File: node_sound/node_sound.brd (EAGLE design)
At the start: 74 x 74 mm, 8 parts, among them U1 TINY85-20-DIP

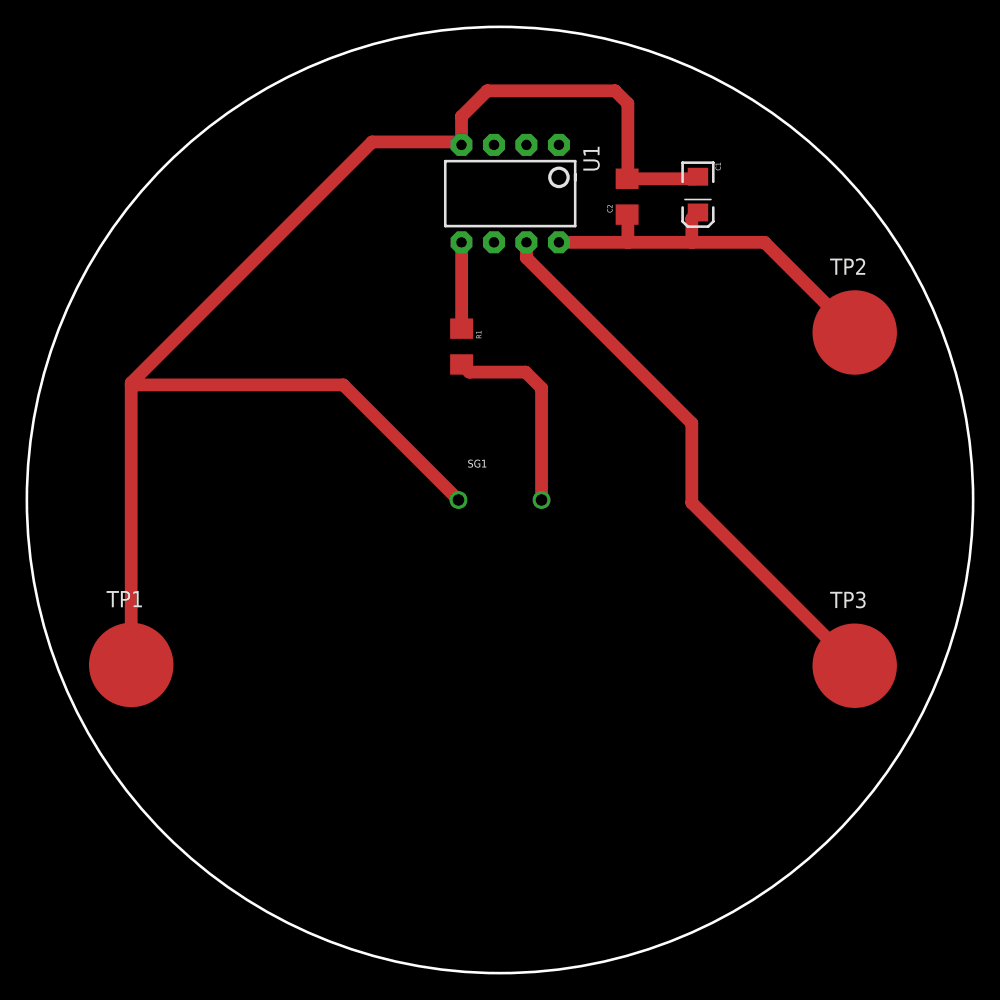
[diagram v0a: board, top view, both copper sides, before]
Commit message: Box dimension added
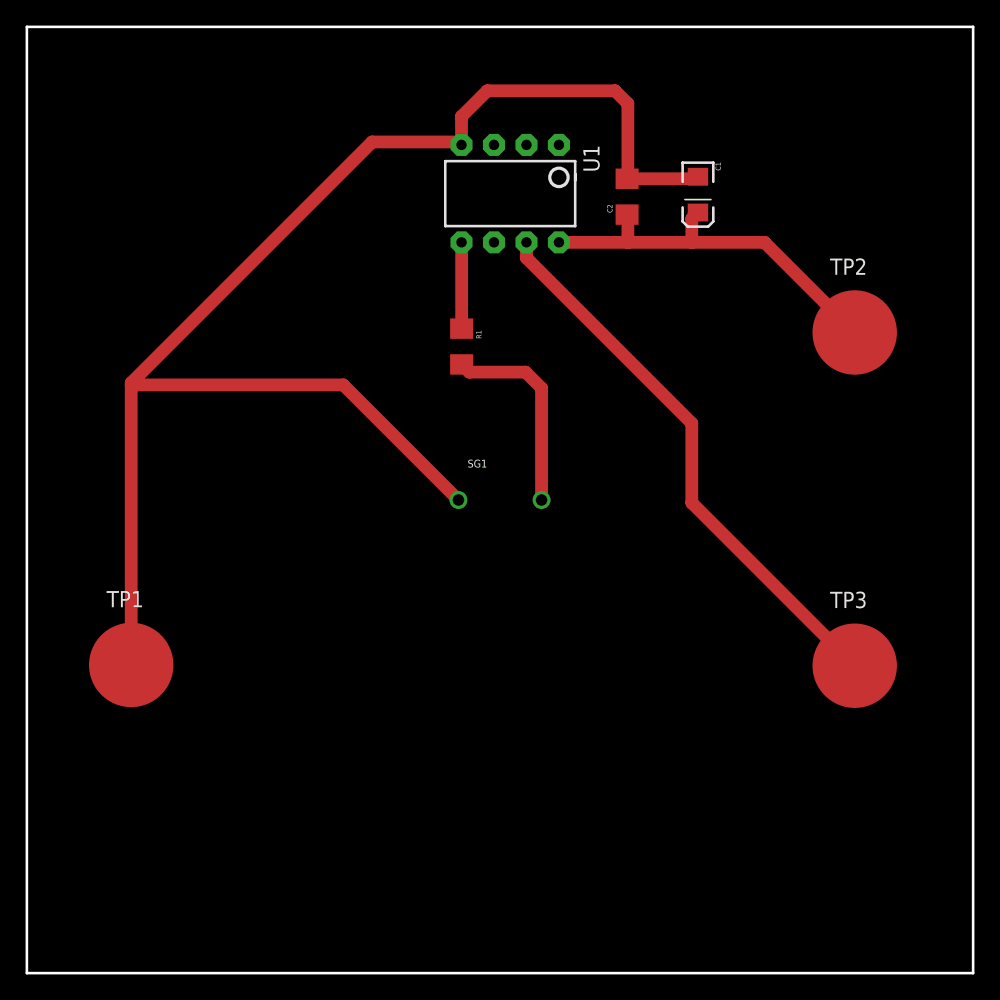
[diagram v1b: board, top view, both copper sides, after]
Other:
- outline, holes or cut-outs redrawn
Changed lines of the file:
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@@
 <layers>
 <layer number="1" name="Top" color="4" fill="1" visible="yes" active="yes"/>
-<layer number="16" name="Bottom" color="1" fill="1" visible="no" active="yes"/>
+<layer number="16" name="Bottom" color="1" fill="1" visible="yes" active="yes"/>
 <layer number="17" name="Pads" color="2" fill="1" visible="yes" active="yes"/>
 <layer number="18" name="Vias" color="2" fill="1" visible="yes" active="yes"/>
@@
 <text x="64" y="63" size="1.9304" layer="114" font="vector">VCC</text>
 <text x="62" y="37" size="1.9304" layer="114" font="vector">DATA</text>
-<circle x="47" y="51" radius="37" width="0.2032" layer="20"/>
+<circle x="47" y="51" radius="37" width="0.2032" layer="114"/>
 <text x="33" y="28" size="3.81" layer="114">♫</text>
 <text x="41" y="33" size="3.81" layer="114">♫</text>
 <text x="49" y="37" size="3.81" layer="114">♫</text>
+<wire x1="84" y1="88" x2="84" y2="14" width="0.2032" layer="20"/>
+<wire x1="84" y1="14" x2="10" y2="14" width="0.2032" layer="20"/>
+<wire x1="10" y1="14" x2="10" y2="88" width="0.2032" layer="20"/>
+<wire x1="10" y1="88" x2="84" y2="88" width="0.2032" layer="20"/>
 </plain>
 <attributes>
